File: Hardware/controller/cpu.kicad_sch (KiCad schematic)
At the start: 34 parts, among them J301 Conn_ARM_JTAG_SWD_10, J302 Conn_01x03_Male, SW301 B3F-1005, SW302 B3F-1002, U302 ATSAME51J20A-A, U303 AT25SF321B-SSHB, Y301 32.768kHz, Y302 12MHz

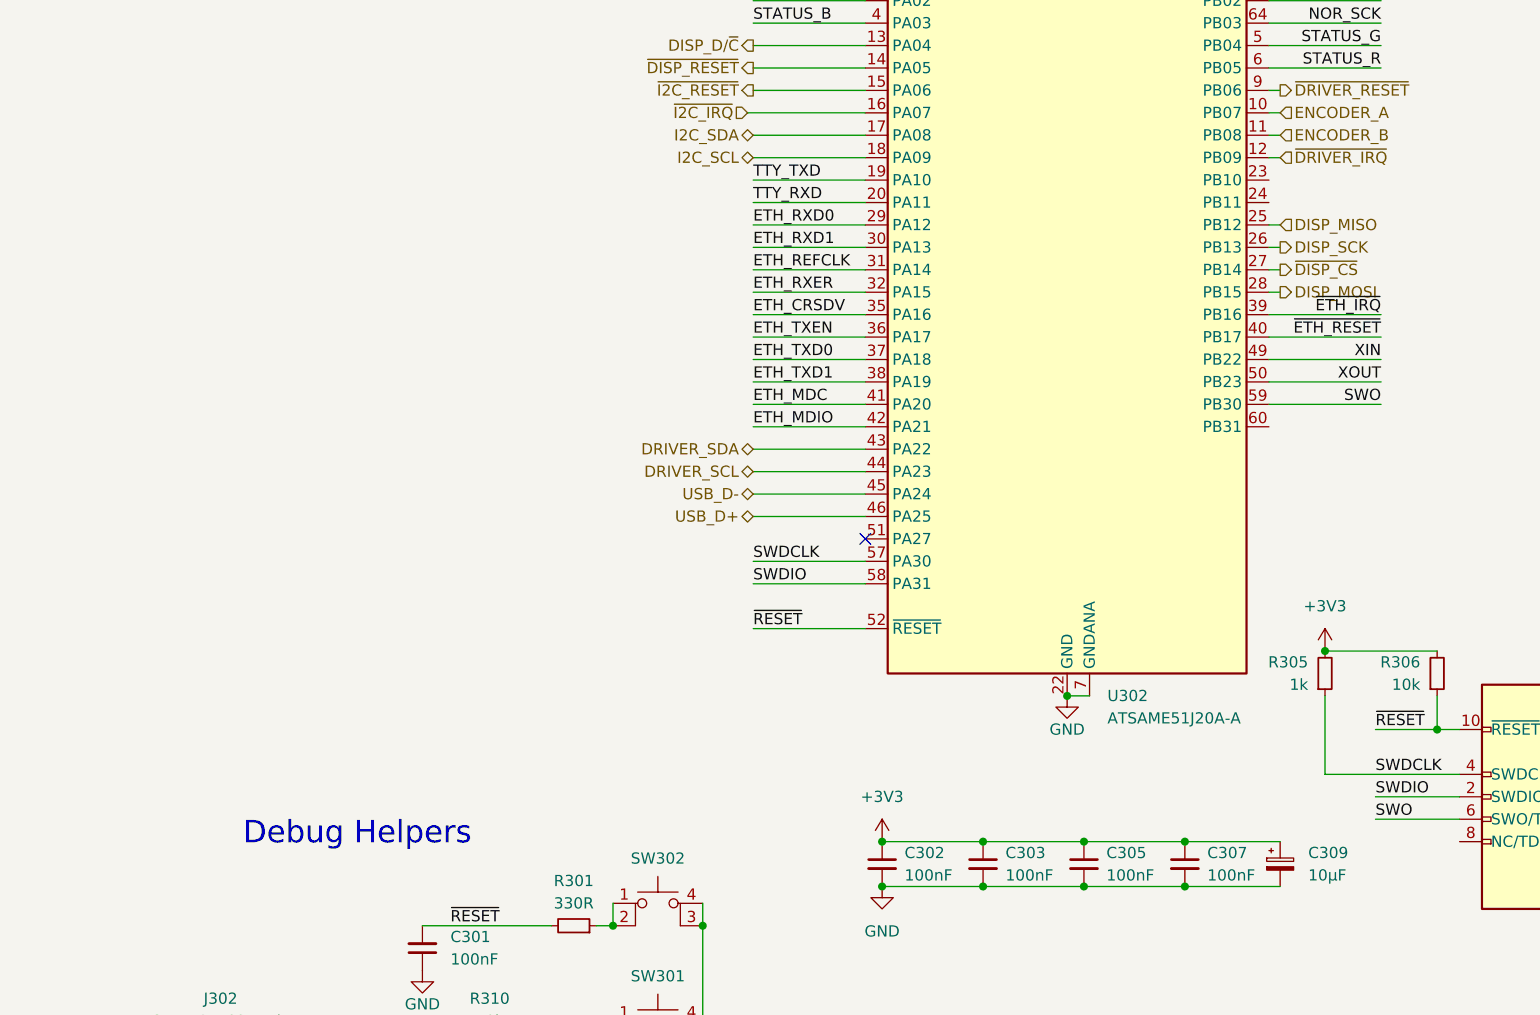
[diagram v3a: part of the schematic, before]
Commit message: Power button on controller board
- Added a power button (with combination white/amber LED) to the
  controller board; it shall poke through the front panel. It's a soft
  power button, so the micro will actually be awake the entire time.
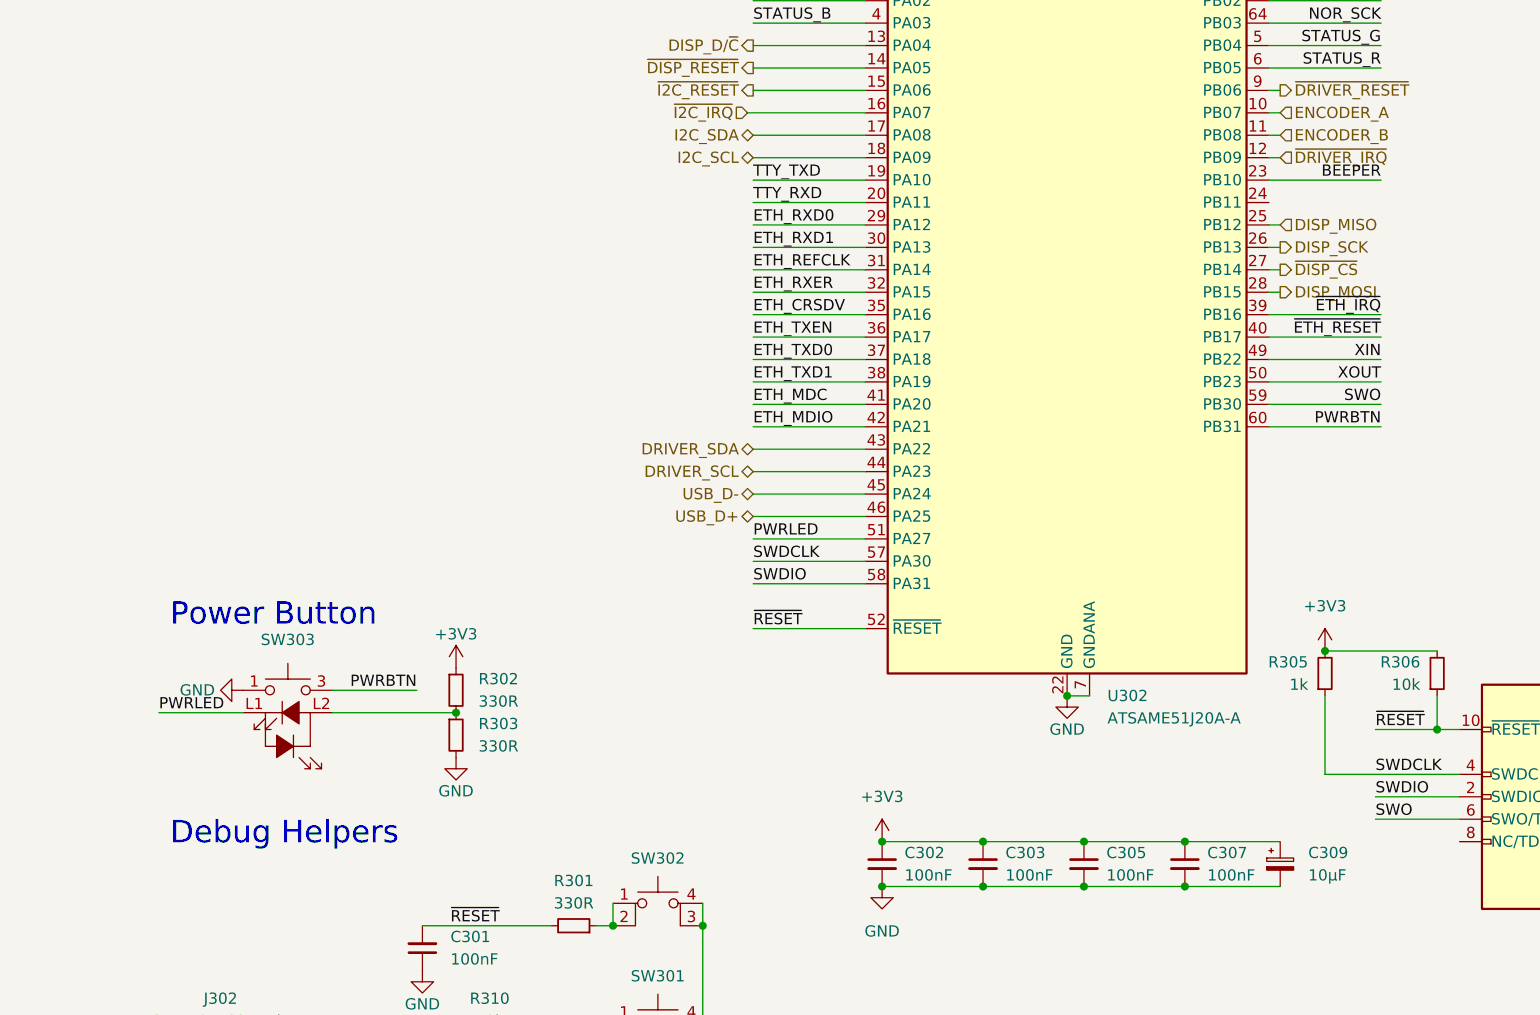
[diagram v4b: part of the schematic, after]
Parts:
- added R302, R303: 330R, Resistor_SMD:R_0805_2012Metric_Pad1.20x1.40mm_HandSolder, symbol Device:R_Small
- added SW303: 228ADS2AAWFCMBA, programmable-load:CTS-228ADS2, symbol programmable-load:CTS-228ADS2
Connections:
- net +3V3: now also R302.1
- net GND: now also R303.2, SW303.1, SW303.2 (1)
- net BEEPER: now reaches U302.23 (PB10)
- net PWRLED: now reaches U302.51 (PA27)
- net PWRLED: now also SW303.L1
- net PWRBTN: now reaches U302.60 (PB31)
- net PWRBTN: now also SW303.3 (2), SW303.4 (2)
- new net: R302.2, R303.1, SW303.L2
- no-connect marks 1 -> 0
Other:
- note added: "Power Button"
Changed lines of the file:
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@@
   (junction (at 190.5 148.59) (diameter 0) (color 0 0 0 0)
   )
+  (junction (at 142.24 133.985) (diameter 0) (color 0 0 0 0)
+  )
   (junction (at 230.505 31.115) (diameter 0) (color 0 0 0 0)
   )
   (junction (at 201.93 153.67) (diameter 0) (color 0 0 0 0)
   )
-  (no_connect (at 188.595 114.3))
   (wire (pts (xy 38.1 123.825) (xy 39.37 123.825))
     (stroke (width 0) (type default) (color 0 0 0 0))
@@
     (stroke (width 0) (type default) (color 0 0 0 0))
   )
+  (wire (pts (xy 137.795 131.445) (xy 128.27 131.445))
+    (stroke (width 0) (type default) (color 0 0 0 0))
+  )
   (wire (pts (xy 19.05 25.4) (xy 22.225 25.4))
     (stroke (width 0) (type default) (color 0 0 0 0))
@@
     (stroke (width 0) (type default) (color 0 0 0 0))
   )
+  (wire (pts (xy 234.315 101.6) (xy 247.015 101.6))
+    (stroke (width 0) (type default) (color 0 0 0 0))
+  )
   (wire (pts (xy 160.02 155.575) (xy 160.02 158.115))
     (stroke (width 0) (type default) (color 0 0 0 0))
@@
     (stroke (width 0) (type default) (color 0 0 0 0))
   )
+  (wire (pts (xy 175.895 114.3) (xy 188.595 114.3))
+    (stroke (width 0) (type default) (color 0 0 0 0))
+  )
   (wire (pts (xy 38.1 74.295) (xy 50.8 74.295))
     (stroke (width 0) (type default) (color 0 0 0 0))
@@
     (stroke (width 0) (type default) (color 0 0 0 0))
   )
+  (wire (pts (xy 234.315 73.66) (xy 247.015 73.66))
+    (stroke (width 0) (type default) (color 0 0 0 0))
+  )
   (wire (pts (xy 230.505 36.195) (xy 241.3 36.195))
     (stroke (width 0) (type default) (color 0 0 0 0))
@@
     (stroke (width 0) (type default) (color 0 0 0 0))
   )
+  (wire (pts (xy 108.585 133.985) (xy 118.11 133.985))
+    (stroke (width 0) (type default) (color 0 0 0 0))
+  )
   (wire (pts (xy 160.02 168.91) (xy 160.02 171.45))
     (stroke (width 0) (type default) (color 0 0 0 0))
@@
     (stroke (width 0) (type default) (color 0 0 0 0))
   )
+  (wire (pts (xy 128.27 133.985) (xy 142.24 133.985))
+    (stroke (width 0) (type default) (color 0 0 0 0))
+  )
   (wire (pts (xy 175.895 68.58) (xy 188.595 68.58))
     (stroke (width 0) (type default) (color 0 0 0 0))
@@
     (stroke (width 0) (type default) (color 0 0 0 0))
   )
-  (text "Debug Helpers" (at 118.11 149.225 0)
+  (text "Debug Helpers" (at 109.855 149.225 0)
+    (effects (font (size 2.54 2.54)) (justify left bottom))
+  )
+  (text "Power Button" (at 109.855 124.46 0)
     (effects (font (size 2.54 2.54)) (justify left bottom))
   )
@@
     (effects (font (size 1.27 1.27)) (justify left bottom))
   )
+  (label "PWRLED" (at 175.895 114.3 0)
+    (effects (font (size 1.27 1.27)) (justify left bottom))
+  )
   (label "SWDIO" (at 175.895 119.38 0)
     (effects (font (size 1.27 1.27)) (justify left bottom))
   )
+  (label "PWRLED" (at 108.585 133.985 0)
+    (effects (font (size 1.27 1.27)) (justify left bottom))
+  )
   (label "ETH_CRSDV" (at 175.895 88.9 0)
     (effects (font (size 1.27 1.27)) (justify left bottom))
@@
     (effects (font (size 1.27 1.27)) (justify left bottom))
   )
+  (label "BEEPER" (at 247.015 73.66 180)
+    (effects (font (size 1.27 1.27)) (justify right bottom))
+  )
   (label "STATUS_G" (at 247.015 58.42 180)
     (effects (font (size 1.27 1.27)) (justify right bottom))
@@
     (effects (font (size 1.27 1.27)) (justify left bottom))
   )
+  (label "PWRBTN" (at 247.015 101.6 180)
+    (effects (font (size 1.27 1.27)) (justify right bottom))
+  )
   (label "ETH_REFCLK" (at 50.8 84.455 180)
     (effects (font (size 1.27 1.27)) (justify right bottom))
@@
   )
   (label "XIN" (at 247.015 93.98 180)
+    (effects (font (size 1.27 1.27)) (justify right bottom))
+  )
+  (label "PWRBTN" (at 137.795 131.445 180)
     (effects (font (size 1.27 1.27)) (justify right bottom))
   )
@@
     (pin "1")
   )
+  (symbol (lib_id "power:GND") (at 142.24 139.065 0) (unit 1)
+    (in_bom yes) (on_board yes)
+    (property "Reference" "#PWR0304" (id 0) (at 142.24 145.415 0)
+      (effects (font (size 1.27 1.27)) hide)
+    )
+    (property "Value" "GND" (id 1) (at 142.24 142.875 0))
+    (property "Footprint" "" (id 2) (at 142.24 139.065 0)
+      (effects (font (size 1.27 1.27)) hide)
+    )
+    (property "Datasheet" "" (id 3) (at 142.24 139.065 0)
+      (effects (font (size 1.27 1.27)) hide)
+    )
+    (pin "1")
+  )
   (symbol (lib_id "power:+3V3") (at 58.42 166.37 0) (unit 1)
     (in_bom yes) (on_board yes)
@@
     (pin "1")
     (pin "2")
+  )
+  (symbol (lib_id "power:GND") (at 118.11 131.445 270) (unit 1)
+    (in_bom yes) (on_board yes) (fields_autoplaced)
+    (property "Reference" "#PWR0302" (id 0) (at 111.76 131.445 0)
+      (effects (font (size 1.27 1.27)) hide)
+    )
+    (property "Value" "GND" (id 1) (at 114.935 131.4449 90)
+      (effects (font (size 1.27 1.27)) (justify right))
+    )
+    (property "Footprint" "" (id 2) (at 118.11 131.445 0)
+      (effects (font (size 1.27 1.27)) hide)
+    )
+    (property "Datasheet" "" (id 3) (at 118.11 131.445 0)
+      (effects (font (size 1.27 1.27)) hide)
+    )
+    (pin "1")
   )
   (symbol (lib_id "Device:R_Small") (at 146.05 171.45 270) (mirror x) (unit 1)
@@
     (pin "1")
   )
+  (symbol (lib_id "Device:R_Small") (at 142.24 131.445 0) (unit 1)
+    (in_bom yes) (on_board yes) (fields_autoplaced)
+    (property "Reference" "R302" (id 0) (at 144.78 130.1749 0)
+      (effects (font (size 1.27 1.27)) (justify left))
+    )
+    (property "Value" "330R" (id 1) (at 144.78 132.7149 0)
+      (effects (font (size 1.27 1.27)) (justify left))
+    )
+    (property "Footprint" "Resistor_SMD:R_0805_2012Metric_Pad1.20x1.40mm_HandSolder" (id 2) (at 142.24 131.445 0)
+      (effects (font (size 1.27 1.27)) hide)
+    )
+    (property "Datasheet" "~" (id 3) (at 142.24 131.445 0)
+      (effects (font (size 1.27 1.27)) hide)
+    )
+    (property "MPn" "RMC1/10-103JTP" (id 4) (at 142.24 131.445 0)
+      (effects (font (size 1.27 1.27)) hide)
+    )
+    (pin "1")
+    (pin "2")
+  )
   (symbol (lib_id "programmable-load:AT25SF321B-SSHB") (at 58.42 179.07 0) (unit 1)
     (in_bom yes) (on_board yes)
@@
     (pin "2")
     (pin "3")
+  )
+  (symbol (lib_id "power:+3V3") (at 142.24 128.905 0) (unit 1)
+    (in_bom yes) (on_board yes)
+    (property "Reference" "#PWR0303" (id 0) (at 142.24 132.715 0)
+      (effects (font (size 1.27 1.27)) hide)
+    )
+    (property "Value" "+3V3" (id 1) (at 142.24 125.095 0))
+    (property "Footprint" "" (id 2) (at 142.24 128.905 0)
+      (effects (font (size 1.27 1.27)) hide)
+    )
+    (property "Datasheet" "" (id 3) (at 142.24 128.905 0)
+      (effects (font (size 1.27 1.27)) hide)
+    )
+    (pin "1")
   )
   (symbol (lib_id "Device:C_Small") (at 24.765 52.07 90) (unit 1)
@@
     (pin "4")
   )
+  (symbol (lib_id "programmable-load:CTS-228ADS2") (at 123.19 133.985 0) (unit 1)
+    (in_bom yes) (on_board yes) (fields_autoplaced)
+    (property "Reference" "SW303" (id 0) (at 123.19 125.73 0))
+    (property "Value" "228ADS2AAWFCMBA" (id 1) (at 123.19 122.555 0)
+      (effects (font (size 1.27 1.27)) hide)
+    )
+    (property "Footprint" "programmable-load:CTS-228ADS2" (id 2) (at 123.19 126.365 0)
+      (effects (font (size 1.27 1.27)) hide)
+    )
+    (property "Datasheet" "https://www.mouser.com/datasheet/2/96/228A-1371184.pdf" (id 3) (at 123.19 126.365 0)
+      (effects (font (size 1.27 1.27)) hide)
+    )
+    (property "MPN" "228ADS2AAWFCMBA" (id 4) (at 123.19 133.985 0)
+      (effects (font (size 1.27 1.27)) hide)
+    )
+    (pin "1")
+    (pin "2")
+    (pin "3")
+    (pin "4")
+    (pin "L1")
+    (pin "L2")
+  )
   (symbol (lib_id "power:GND") (at 241.3 36.195 0) (unit 1)
     (in_bom yes) (on_board yes)
@@
       (effects (font (size 1.27 1.27)) hide)
     )
+    (pin "1")
+    (pin "2")
+  )
+  (symbol (lib_id "Device:R_Small") (at 142.24 136.525 0) (unit 1)
+    (in_bom yes) (on_board yes) (fields_autoplaced)
+    (property "Reference" "R303" (id 0) (at 144.78 135.2549 0)
+      (effects (font (size 1.27 1.27)) (justify left))
+    )
+    (property "Value" "330R" (id 1) (at 144.78 137.7949 0)
+      (effects (font (size 1.27 1.27)) (justify left))
+    )
+    (property "Footprint" "Resistor_SMD:R_0805_2012Metric_Pad1.20x1.40mm_HandSolder" (id 2) (at 142.24 136.525 0)
+      (effects (font (size 1.27 1.27)) hide)
+    )
+    (property "Datasheet" "~" (id 3) (at 142.24 136.525 0)
+      (effects (font (size 1.27 1.27)) hide)
+    )
+    (property "MPn" "RMC1/10-103JTP" (id 4) (at 142.24 136.525 0)
+      (effects (font (size 1.27 1.27)) hide)
+    )

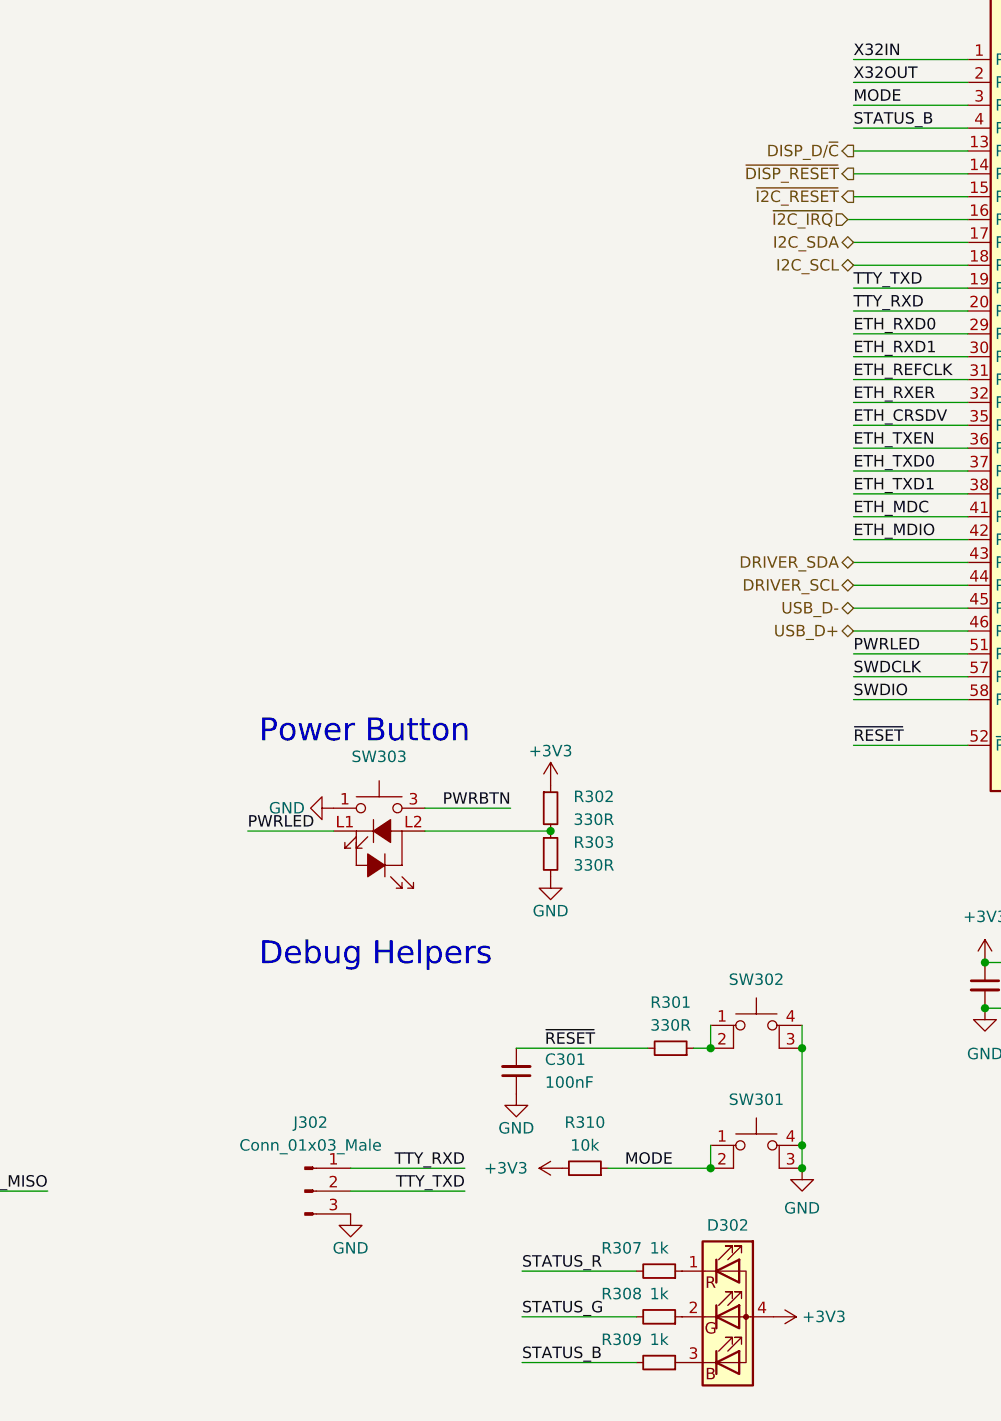
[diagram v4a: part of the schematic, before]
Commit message: Added beeper to control board
- Added a beeper (magnetic transducer, including an amplifier to go with
  it) to the controller board so we can make loud annoying beeping
  noises as desired

- A few minor tweaks to the layout of the control board
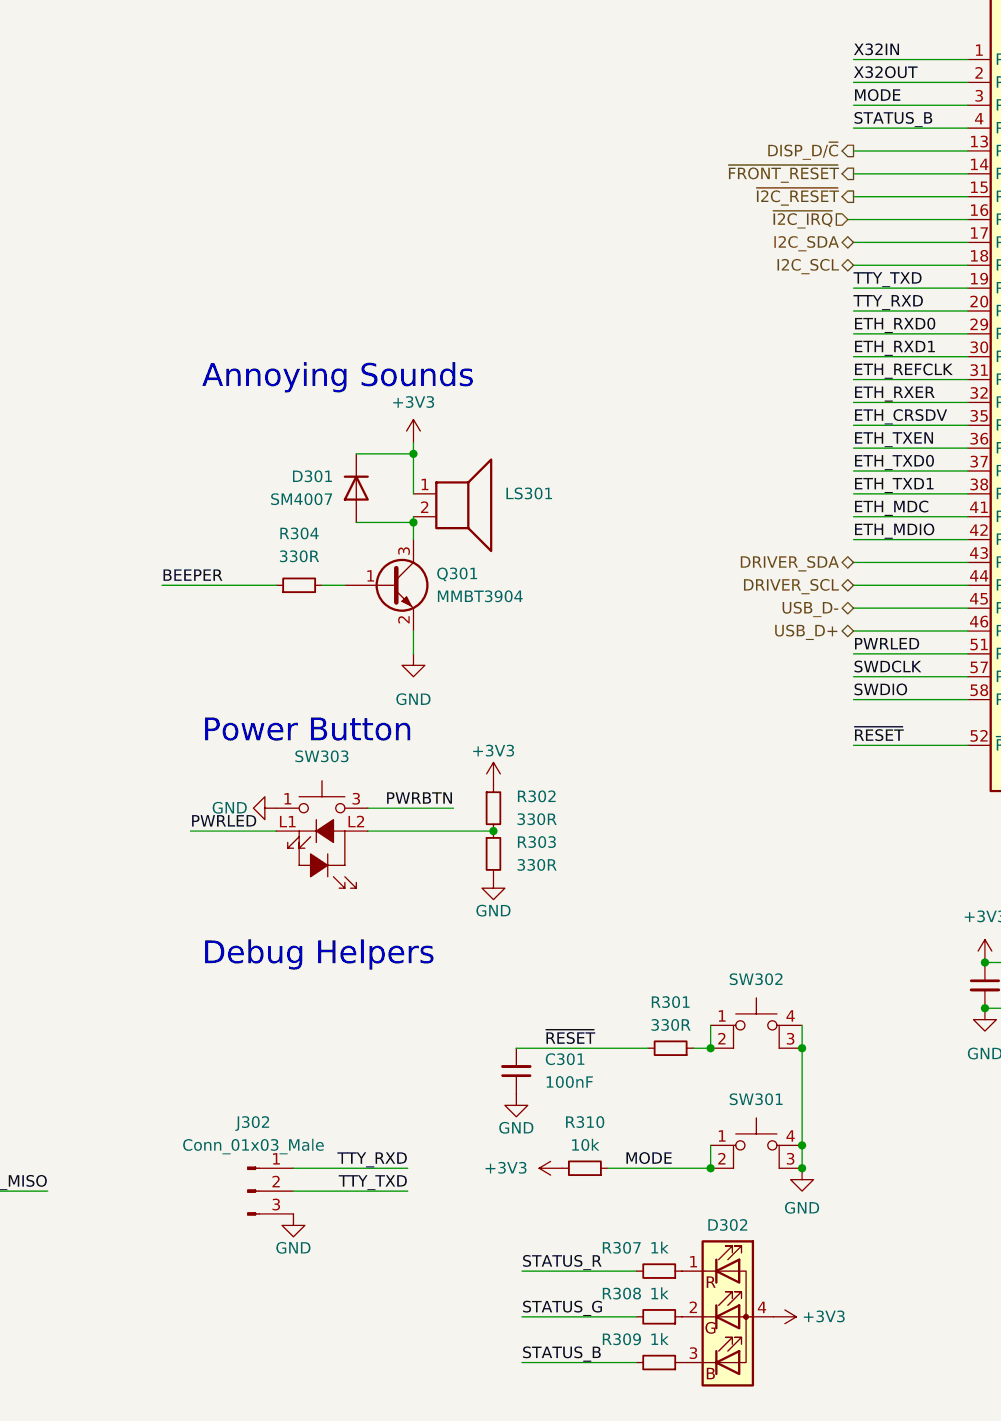
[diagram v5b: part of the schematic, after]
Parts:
- added D301: SM4007, Diode_SMD:D_SMA_Handsoldering, symbol Diode:SM4007
- added LS301: Speaker, programmable-load:PUI-AT-1224-TWT, symbol Device:Speaker
- added Q301: MMBT3904, Package_TO_SOT_SMD:SOT-23, symbol Transistor_BJT:MMBT3904
- added R304: 330R, Resistor_SMD:R_0805_2012Metric_Pad1.20x1.40mm_HandSolder, symbol Device:R_Small
- R301: MPN RMC1/10-103JTP -> RMC1/10-331JTP
- R302, R303: MPn RMC1/10-103JTP -> RMC1/10-331JTP
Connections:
- net +3V3: now also D301.1 (K), LS301.1
- net BEEPER: now also R304.1
- net GND: now also Q301.2 (E)
- net ~{DISP_RESET} renamed ~{FRONT_RESET}
- new net: Q301.1 (B), R304.2
- new net: D301.2 (A), LS301.2, Q301.3 (C)
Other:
- note added: "Annoying Sounds"
- moved on the sheet: J302, R302, R303, SW303
